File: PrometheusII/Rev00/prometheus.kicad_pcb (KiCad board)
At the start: 4 copper layers, 223.5 x 222.3 mm, 196 parts, among them J1 0878311420, J10 Conn_02x02_Odd_Even, J11 Conn_02x02_Odd_Even, J16 Conn_02x07_Odd_Even, J17 Conn_02x07_Odd_Even, J18 Conn_02x07_Odd_Even, J19 Conn_02x07_Odd_Even, J2 Conn_02x08_Odd_Even, J3 Conn_02x02_Odd_Even, J4 Conn_02x02_Odd_Even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

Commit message: placement tuning
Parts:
- moved R71 0.51 mm to (217.1, 109.6)
- moved R74 0.51 mm to (215.6, 109.6)
- moved R62 0.08 mm to (210.9, 104.2)
- moved R65 0.08 mm to (213.8, 104.2)
- moved C34 0.08 mm to (212.4, 105.7)
- moved R72 0.08 mm to (216.8, 104.2)
- moved C39 0.05 mm to (210.5, 110.6)
- moved R75 0.05 mm to (209.0, 110.6)
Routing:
- net GND: track 15.3 -> 10.3 mm
- net +3V3: track 8.67 -> 6.85 mm
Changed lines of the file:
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@@
     (thickness 1.6)
     (drawings 40)
-    (tracks 69)
+    (tracks 62)
     (zones 0)
     (modules 196)
@@
   )
   (module Resistor_SMD:R_0603_1608Metric (layer B.Cu)
-    (at 208.9911 110.6678 270)
+    (at 208.9911 110.617 270)
     (descr "Resistor SMD 0603 (1608 Metric), square (rectangular) end terminal, IPC_7351 nominal, (Body size source: http://www.tortai-tech.com/upload/download/2011102023233369053.pdf), generated with kicad-footprint-generator")
     (tags resistor)
@@
   )
   (module Resistor_SMD:R_0603_1608Metric (layer B.Cu)
-    (at 215.5951 110.0963 90)
+    (at 215.6059 109.5847 90)
     (descr "Resistor SMD 0603 (1608 Metric), square (rectangular) end terminal, IPC_7351 nominal, (Body size source: http://www.tortai-tech.com/upload/download/2011102023233369053.pdf), generated with kicad-footprint-generator")
     (tags resistor)
@@
   )
   (module Resistor_SMD:R_0603_1608Metric (layer B.Cu)
-    (at 209.6896 108.4453 180)
+    (at 209.7023 108.4072 180)
     (descr "Resistor SMD 0603 (1608 Metric), square (rectangular) end terminal, IPC_7351 nominal, (Body size source: http://www.tortai-tech.com/upload/download/2011102023233369053.pdf), generated with kicad-footprint-generator")
     (tags resistor)
@@
   )
   (module Resistor_SMD:R_0603_1608Metric (layer B.Cu)
-    (at 216.7127 104.1908)
+    (at 216.7927 104.1908)
     (descr "Resistor SMD 0603 (1608 Metric), square (rectangular) end terminal, IPC_7351 nominal, (Body size source: http://www.tortai-tech.com/upload/download/2011102023233369053.pdf), generated with kicad-footprint-generator")
     (tags resistor)
@@
   )
   (module Resistor_SMD:R_0603_1608Metric (layer B.Cu)
-    (at 217.0556 110.0963 270)
+    (at 217.0664 109.5847 270)
     (descr "Resistor SMD 0603 (1608 Metric), square (rectangular) end terminal, IPC_7351 nominal, (Body size source: http://www.tortai-tech.com/upload/download/2011102023233369053.pdf), generated with kicad-footprint-generator")
     (tags resistor)
@@
   )
   (module Resistor_SMD:R_0603_1608Metric (layer B.Cu)
-    (at 217.4366 114.9858)
+    (at 217.4766 114.9858)
     (descr "Resistor SMD 0603 (1608 Metric), square (rectangular) end terminal, IPC_7351 nominal, (Body size source: http://www.tortai-tech.com/upload/download/2011102023233369053.pdf), generated with kicad-footprint-generator")
     (tags resistor)
@@
   )
   (module Resistor_SMD:R_0603_1608Metric (layer B.Cu)
-    (at 213.7663 104.1908)
+    (at 213.8463 104.1908)
     (descr "Resistor SMD 0603 (1608 Metric), square (rectangular) end terminal, IPC_7351 nominal, (Body size source: http://www.tortai-tech.com/upload/download/2011102023233369053.pdf), generated with kicad-footprint-generator")
     (tags resistor)
@@
   )
   (module Resistor_SMD:R_0603_1608Metric (layer B.Cu)
-    (at 214.4521 114.9858)
+    (at 214.4921 114.9858)
     (descr "Resistor SMD 0603 (1608 Metric), square (rectangular) end terminal, IPC_7351 nominal, (Body size source: http://www.tortai-tech.com/upload/download/2011102023233369053.pdf), generated with kicad-footprint-generator")
     (tags resistor)
@@
   )
   (module Resistor_SMD:R_0603_1608Metric (layer B.Cu)
-    (at 210.8199 104.1908 180)
+    (at 210.8999 104.1908 180)
     (descr "Resistor SMD 0603 (1608 Metric), square (rectangular) end terminal, IPC_7351 nominal, (Body size source: http://www.tortai-tech.com/upload/download/2011102023233369053.pdf), generated with kicad-footprint-generator")
     (tags resistor)
@@
   )
   (module Resistor_SMD:R_0603_1608Metric (layer B.Cu)
-    (at 211.4676 114.9858 180)
+    (at 211.5076 114.9858 180)
     (descr "Resistor SMD 0603 (1608 Metric), square (rectangular) end terminal, IPC_7351 nominal, (Body size source: http://www.tortai-tech.com/upload/download/2011102023233369053.pdf), generated with kicad-footprint-generator")
     (tags resistor)
@@
   )
   (module Capacitor_SMD:C_0603_1608Metric (layer B.Cu)
-    (at 210.4516 110.6678 270)
+    (at 210.4516 110.617 270)
     (descr "Capacitor SMD 0603 (1608 Metric), square (rectangular) end terminal, IPC_7351 nominal, (Body size source: http://www.tortai-tech.com/upload/download/2011102023233369053.pdf), generated with kicad-footprint-generator")
     (tags capacitor)
@@
   )
   (module Capacitor_SMD:C_0603_1608Metric (layer B.Cu)
-    (at 212.2931 105.6513 180)
+    (at 212.3731 105.6513 180)
     (descr "Capacitor SMD 0603 (1608 Metric), square (rectangular) end terminal, IPC_7351 nominal, (Body size source: http://www.tortai-tech.com/upload/download/2011102023233369053.pdf), generated with kicad-footprint-generator")
     (tags capacitor)
@@
   )
   (module Capacitor_SMD:C_0603_1608Metric (layer B.Cu)
-    (at 212.9916 113.5126 180)
+    (at 213.0316 113.5126 180)
     (descr "Capacitor SMD 0603 (1608 Metric), square (rectangular) end terminal, IPC_7351 nominal, (Body size source: http://www.tortai-tech.com/upload/download/2011102023233369053.pdf), generated with kicad-footprint-generator")
     (tags capacitor)
@@
   (segment (start 173.656 112.902) (end 174.1955 113.4415) (width 0.1524) (layer B.Cu) (net 1))
   (segment (start 173.656 111.9295) (end 173.656 112.902) (width 0.1524) (layer B.Cu) (net 1))
-  (segment (start 214.0048 108.2657) (end 214.0048 107.3883) (width 0.1524) (layer B.Cu) (net 1))
-  (segment (start 214.0048 108.3211) (end 214.0048 108.2657) (width 0.1524) (layer B.Cu) (net 1))
-  (segment (start 212.6361 109.6898) (end 214.0048 108.3211) (width 0.1524) (layer B.Cu) (net 1))
-  (segment (start 210.4516 109.6898) (end 212.6361 109.6898) (width 0.1524) (layer B.Cu) (net 1))
   (segment (start 175.799999 122.040999) (end 176.3395 122.5805) (width 0.1524) (layer B.Cu) (net 6))
   (segment (start 174.846501 122.040999) (end 175.799999 122.040999) (width 0.1524) (layer B.Cu) (net 6))
@@
   (segment (start 173.156 112.906) (end 172.6205 113.4415) (width 0.1524) (layer B.Cu) (net 7))
   (segment (start 173.156 111.9295) (end 173.156 112.906) (width 0.1524) (layer B.Cu) (net 7))
-  (segment (start 211.5501 111.7883) (end 212.0548 111.7883) (width 0.1524) (layer B.Cu) (net 7))
-  (segment (start 210.4516 111.2648) (end 211.0266 111.2648) (width 0.1524) (layer B.Cu) (net 7))
-  (segment (start 211.0266 111.2648) (end 211.5501 111.7883) (width 0.1524) (layer B.Cu) (net 7))
   (segment (start 173.975917 118.687389) (end 176.383389 118.687389) (width 0.1524) (layer B.Cu) (net 42))
   (segment (start 173.659001 119.353499) (end 173.659001 119.004305) (width 0.1524) (layer B.Cu) (net 42))

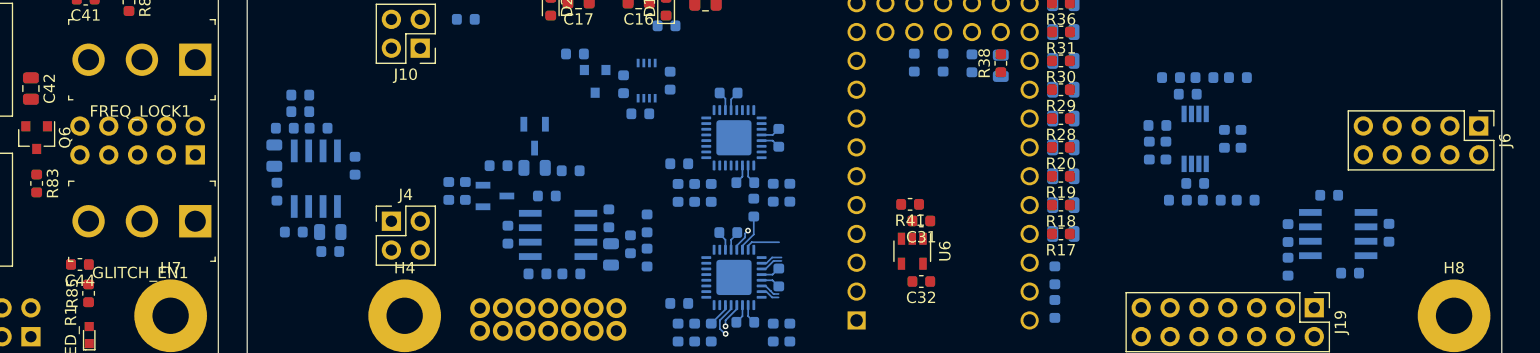
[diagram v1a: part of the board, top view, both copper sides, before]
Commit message: Fixed connector placement
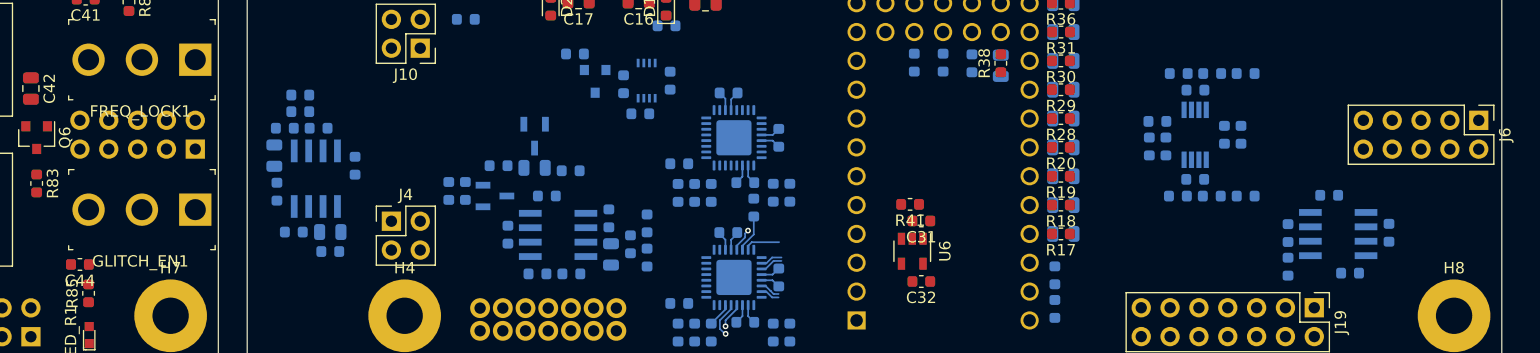
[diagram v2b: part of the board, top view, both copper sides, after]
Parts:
- moved GLITCH_EN1 1.02 mm to (125.0, 115.8)
- moved C34 0.77 mm to (213.1, 105.3)
- moved R62 0.77 mm to (211.6, 103.8)
- moved R72 0.77 mm to (217.5, 103.8)
- moved R65 0.77 mm to (214.5, 103.8)
- moved J5 0.51 mm to (125.0, 110.5)
- moved J6 0.50 mm to (238.0, 108.0)
- moved C33 0.36 mm to (213.0, 113.2)
- moved C39 0.36 mm to (210.5, 110.3)
- moved R60 0.36 mm to (211.5, 114.6)
- moved R64 0.36 mm to (214.5, 114.6)
- moved R70 0.36 mm to (217.5, 114.6)
- moved R71 0.36 mm to (217.1, 109.2)
- moved R73 0.36 mm to (209.7, 108.0)
- moved R74 0.36 mm to (215.6, 109.2)
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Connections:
- U1 pad 36: /LFSR0_IN -> /TAPS_LED_T
- U1 pad 37: /LFSR1_IN -> /LFO_LED_T
- U1 pad 38: /LFO_LED_T -> /EXT_CLK_EN_T
- U1 pad 39: /TAPS_LED_T -> /LFSR0_IN
- U1 pad 44: /EXT_CLK_EN_T -> /LFSR1_IN
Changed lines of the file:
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@@
     )
   )
-  (module Connector_PinHeader_2.54mm:PinHeader_2x05_P2.54mm_Vertical (layer F.Cu)
-    (at 238.004 108.452 270)
+  (module Connector_PinHeader_2.54mm:PinHeader_2x05_P2.54mm_Vertical locked (layer F.Cu)
+    (at 238.004 107.952 270)
     (descr "Through hole straight pin header, 2x05, 2.54mm pitch, double rows")
     (tags "Through hole pin header THT 2x05 2.54mm double row")
@@
   )
   (module Connector_PinHeader_2.54mm:PinHeader_2x05_P2.54mm_Vertical locked (layer B.Cu)
-    (at 124.968 110.999 90)
+    (at 124.968 110.489 90)
     (descr "Through hole straight pin header, 2x05, 2.54mm pitch, double rows")
     (tags "Through hole pin header THT 2x05 2.54mm double row")
@@
       (net 10 /CV_FILT))
   )
-  (module Package_SO:MSOP-8_3x3mm_P0.65mm (layer B.Cu)
-    (at 213.0298 109.5883 270)
+  (module Package_SO:MSOP-8_3x3mm_P0.65mm locked (layer B.Cu)
+    (at 213.0298 109.2283 270)
     (descr "8-Lead Plastic Micro Small Outline Package (MS) [MSOP] (see Microchip Packaging Specification 00000049BS.pdf)")
     (tags "SSOP 0.65")
@@
     )
   )
-  (module Resistor_SMD:R_0603_1608Metric (layer B.Cu)
-    (at 208.9911 110.617 270)
+  (module Resistor_SMD:R_0603_1608Metric locked (layer B.Cu)
+    (at 208.9911 110.257 270)
     (descr "Resistor SMD 0603 (1608 Metric), square (rectangular) end terminal, IPC_7351 nominal, (Body size source: http://www.tortai-tech.com/upload/download/2011102023233369053.pdf), generated with kicad-footprint-generator")
     (tags resistor)
@@
     )
   )
-  (module Resistor_SMD:R_0603_1608Metric (layer B.Cu)
-    (at 215.6059 109.5847 90)
+  (module Resistor_SMD:R_0603_1608Metric locked (layer B.Cu)
+    (at 215.6059 109.2247 90)
     (descr "Resistor SMD 0603 (1608 Metric), square (rectangular) end terminal, IPC_7351 nominal, (Body size source: http://www.tortai-tech.com/upload/download/2011102023233369053.pdf), generated with kicad-footprint-generator")
     (tags resistor)
@@
     )
   )
-  (module Resistor_SMD:R_0603_1608Metric (layer B.Cu)
-    (at 209.7023 108.4072 180)
+  (module Resistor_SMD:R_0603_1608Metric locked (layer B.Cu)
+    (at 209.7023 108.0472 180)
     (descr "Resistor SMD 0603 (1608 Metric), square (rectangular) end terminal, IPC_7351 nominal, (Body size source: http://www.tortai-tech.com/upload/download/2011102023233369053.pdf), generated with kicad-footprint-generator")
     (tags resistor)
@@
     )
   )
-  (module Resistor_SMD:R_0603_1608Metric (layer B.Cu)
-    (at 216.7927 104.1908)
+  (module Resistor_SMD:R_0603_1608Metric locked (layer B.Cu)
+    (at 217.4727 103.8308)
     (descr "Resistor SMD 0603 (1608 Metric), square (rectangular) end terminal, IPC_7351 nominal, (Body size source: http://www.tortai-tech.com/upload/download/2011102023233369053.pdf), generated with kicad-footprint-generator")
     (tags resistor)
@@
     )
   )
-  (module Resistor_SMD:R_0603_1608Metric (layer B.Cu)
-    (at 217.0664 109.5847 270)
+  (module Resistor_SMD:R_0603_1608Metric locked (layer B.Cu)
+    (at 217.0664 109.2247 270)
     (descr "Resistor SMD 0603 (1608 Metric), square (rectangular) end terminal, IPC_7351 nominal, (Body size source: http://www.tortai-tech.com/upload/download/2011102023233369053.pdf), generated with kicad-footprint-generator")
     (tags resistor)
@@
     )
   )
-  (module Resistor_SMD:R_0603_1608Metric (layer B.Cu)
-    (at 217.4766 114.9858)
+  (module Resistor_SMD:R_0603_1608Metric locked (layer B.Cu)
+    (at 217.4766 114.6258)
     (descr "Resistor SMD 0603 (1608 Metric), square (rectangular) end terminal, IPC_7351 nominal, (Body size source: http://www.tortai-tech.com/upload/download/2011102023233369053.pdf), generated with kicad-footprint-generator")
     (tags resistor)
@@
     )
   )
-  (module Resistor_SMD:R_0603_1608Metric (layer B.Cu)
-    (at 213.8463 104.1908)
+  (module Resistor_SMD:R_0603_1608Metric locked (layer B.Cu)
+    (at 214.5263 103.8308)
     (descr "Resistor SMD 0603 (1608 Metric), square (rectangular) end terminal, IPC_7351 nominal, (Body size source: http://www.tortai-tech.com/upload/download/2011102023233369053.pdf), generated with kicad-footprint-generator")
     (tags resistor)
@@
     )
   )
-  (module Resistor_SMD:R_0603_1608Metric (layer B.Cu)
-    (at 214.4921 114.9858)
+  (module Resistor_SMD:R_0603_1608Metric locked (layer B.Cu)
+    (at 214.4921 114.6258)
     (descr "Resistor SMD 0603 (1608 Metric), square (rectangular) end terminal, IPC_7351 nominal, (Body size source: http://www.tortai-tech.com/upload/download/2011102023233369053.pdf), generated with kicad-footprint-generator")
     (tags resistor)
@@
     )
   )
-  (module Resistor_SMD:R_0603_1608Metric (layer B.Cu)
-    (at 210.8999 104.1908 180)
+  (module Resistor_SMD:R_0603_1608Metric locked (layer B.Cu)
+    (at 211.5799 103.8308 180)
     (descr "Resistor SMD 0603 (1608 Metric), square (rectangular) end terminal, IPC_7351 nominal, (Body size source: http://www.tortai-tech.com/upload/download/2011102023233369053.pdf), generated with kicad-footprint-generator")
     (tags resistor)
@@
     )
   )
-  (module Resistor_SMD:R_0603_1608Metric (layer B.Cu)
-    (at 211.5076 114.9858 180)
+  (module Resistor_SMD:R_0603_1608Metric locked (layer B.Cu)
+    (at 211.5076 114.6258 180)
     (descr "Resistor SMD 0603 (1608 Metric), square (rectangular) end terminal, IPC_7351 nominal, (Body size source: http://www.tortai-tech.com/upload/download/2011102023233369053.pdf), generated with kicad-footprint-generator")
     (tags resistor)
@@
     )
   )
-  (module Capacitor_SMD:C_0603_1608Metric (layer B.Cu)
-    (at 210.4516 110.617 270)
+  (module Capacitor_SMD:C_0603_1608Metric locked (layer B.Cu)
+    (at 210.4516 110.257 270)
     (descr "Capacitor SMD 0603 (1608 Metric), square (rectangular) end terminal, IPC_7351 nominal, (Body size source: http://www.tortai-tech.com/upload/download/2011102023233369053.pdf), generated with kicad-footprint-generator")
     (tags capacitor)
@@
     )
   )
-  (module Capacitor_SMD:C_0603_1608Metric (layer B.Cu)
-    (at 212.3731 105.6513 180)
+  (module Capacitor_SMD:C_0603_1608Metric locked (layer B.Cu)
+    (at 213.0531 105.2913 180)
     (descr "Capacitor SMD 0603 (1608 Metric), square (rectangular) end terminal, IPC_7351 nominal, (Body size source: http://www.tortai-tech.com/upload/download/2011102023233369053.pdf), generated with kicad-footprint-generator")
     (tags capacitor)
@@
   )
   (module digikey-footprints:Toggle_Switch_100SP1T1B4M2QE locked (layer F.Cu)
-    (at 124.968 116.84 180)
+    (at 124.968 115.82 180)
     (descr http://spec_sheets.e-switch.com/specs/T111597.pdf)
     (fp_text reference GLITCH_EN1 (at 4.84 -4.55) (layer F.SilkS)
@@
     )
     (pad 44 thru_hole circle (at 8.89 -5.08 90) (size 1.6 1.6) (drill 1.1) (layers *.Cu *.Mask)
-      (net 60 /EXT_CLK_EN_T))
+      (net 101 /LFSR1_IN))
     (pad 43 thru_hole circle (at 8.89 -2.54 90) (size 1.6 1.6) (drill 1.1) (layers *.Cu *.Mask)
       (net 34 /FREQ_LOCK_T))
@@
       (net 25 /LFO_T))
     (pad 39 thru_hole circle (at 11.43 -5.08 90) (size 1.6 1.6) (drill 1.1) (layers *.Cu *.Mask)
-      (net 100 /TAPS_LED_T))
+      (net 102 /LFSR0_IN))
     (pad 38 thru_hole circle (at 11.43 -2.54 90) (size 1.6 1.6) (drill 1.1) (layers *.Cu *.Mask)
-      (net 99 /LFO_LED_T))
+      (net 60 /EXT_CLK_EN_T))
     (pad 37 thru_hole circle (at 11.43 0 90) (size 1.6 1.6) (drill 1.1) (layers *.Cu *.Mask)
-      (net 101 /LFSR1_IN))
+      (net 99 /LFO_LED_T))
     (pad 36 thru_hole circle (at 11.43 2.54 90) (size 1.6 1.6) (drill 1.1) (layers *.Cu *.Mask)
-      (net 102 /LFSR0_IN))
+      (net 100 /TAPS_LED_T))
     (pad 35 thru_hole circle (at 11.43 5.08 90) (size 1.6 1.6) (drill 1.1) (layers *.Cu *.Mask)
       (net 13 /PARAM_0_T))
@@
     )
   )
-  (module Capacitor_SMD:C_0603_1608Metric (layer B.Cu)
-    (at 213.0316 113.5126 180)
+  (module Capacitor_SMD:C_0603_1608Metric locked (layer B.Cu)
+    (at 213.0316 113.1526 180)
     (descr "Capacitor SMD 0603 (1608 Metric), square (rectangular) end terminal, IPC_7351 nominal, (Body size source: http://www.tortai-tech.com/upload/download/2011102023233369053.pdf), generated with kicad-footprint-generator")
     (tags capacitor)

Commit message: more pinout work
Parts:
- moved C26 22.9 mm to (201.4, 118.0)
- moved R37 22.9 mm to (201.2, 118.0)
- moved C11 10.2 mm to (201.4, 107.8)
- moved C13 10.2 mm to (201.4, 102.7)
- moved R17 10.2 mm to (201.2, 107.8)
- moved R19 10.2 mm to (201.2, 102.7)
- moved C43 8.40 mm to (195.9, 103.1), turned to 270 degrees
- moved R87 7.98 mm to (195.9, 102.9), turned to 90 degrees
- moved C25 6.30 mm to (195.9, 94.6), turned to 90 degrees
- moved R36 6.01 mm to (195.9, 94.8), turned to 270 degrees
- moved C27 5.90 mm to (201.4, 105.3), turned to 0 degrees
- moved R38 5.78 mm to (201.2, 105.3), turned to 180 degrees
- moved C20 5.08 mm to (201.4, 100.2)
- moved R29 5.08 mm to (201.2, 100.2)
- moved C21 5.08 mm to (201.4, 97.6)
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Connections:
- J18 pad 10: /TAPS_LED_P -> /LEN_KNOB_P
- J18 pad 12: /LEN_KNOB_P -> /VOCT_OCT_P
- J18 pad 14: /VOCT_OCT_P -> /TAPS_LED_P
- J19 pad 11: /LEN_KNOB -> /VOCT_OCT
- J19 pad 13: /VOCT_OCT -> /TAPS_LED_T
- J19 pad 9: /TAPS_LED_T -> /LEN_KNOB
- U1 pad 21: /VOCT_OCT_T -> /VOCT_FINE_T
- U1 pad 22: /VOCT_SEMI_T -> /VOCT_ATV_T
- U1 pad 23: /VOCT_FINE_T -> /VOCT_T
- U1 pad 24: /VOCT_ATV_T -> /PARAM_0_CV_T
- U1 pad 25: /VOCT_T -> /LFO_T
- U1 pad 26: /POLY_T -> /LEN_CV_T
- U1 pad 27: /PARAM_1_T -> /POLY_T
- U1 pad 28: /PARAM_0_CV_T -> /PARAM_1_T
- U1 pad 30: /LEN_CV_T -> /VOCT_OCT_T
- U1 pad 35: /PARAM_0_T -> /VOCT_SEMI_T
- U1 pad 40: /LFO_T -> /PARAM_0_T
